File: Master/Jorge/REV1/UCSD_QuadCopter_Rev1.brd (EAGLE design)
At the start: 71.7 x 73.6 mm, 58 parts, among them J1 ISP, K1 653002114822, K2 653002114822, K3 653002114822, K4 653002114822, U1 ATMEGA128RFA1, U2 TPS73633-DBVT, U3 SI2302CDS-T1-E3, U4 LSM9DS0, U5 SI2302CDS-T1-E3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

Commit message: Uploading Finished QuadCopter PCB REV1
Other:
- board size 71.7 x 73.6 mm -> 99.8 x 99.9 mm
- board text added: "0.276 inch 7.0104 mm"
- board text added: "3.930 inch 99.822 mm"
- board text added: "3.934 inch 99.9236 mm"
- board text added: ">Info Board Name: UCSD QuadCopter Part Number: 0 Number of Layers: 2 Dimension X= 3.930 inch Dimension Y= 3.934 inch Board Material Type: FR-4 Solder Mask Color: Green Silkscreen Color: White Finish Plating: HASAL Revision Number: 1"
- board text removed: "0.238 inch 6.045 mm"
- board text removed: "2.83 inch 71.88 mm"
- board text removed: "2.90 inch 73.66 mm"
- board text removed: ">Info Board Name: UCSD QuadCopter Part Number: 0 Number of Layers: 2 Dimension X= 2.83 inch Dimension Y= 2.90 inch Board Material Type: FR-4 Solder Mask Color: Green Silkscreen Color: White Finish Plating: HASAL Revision Number: 1"

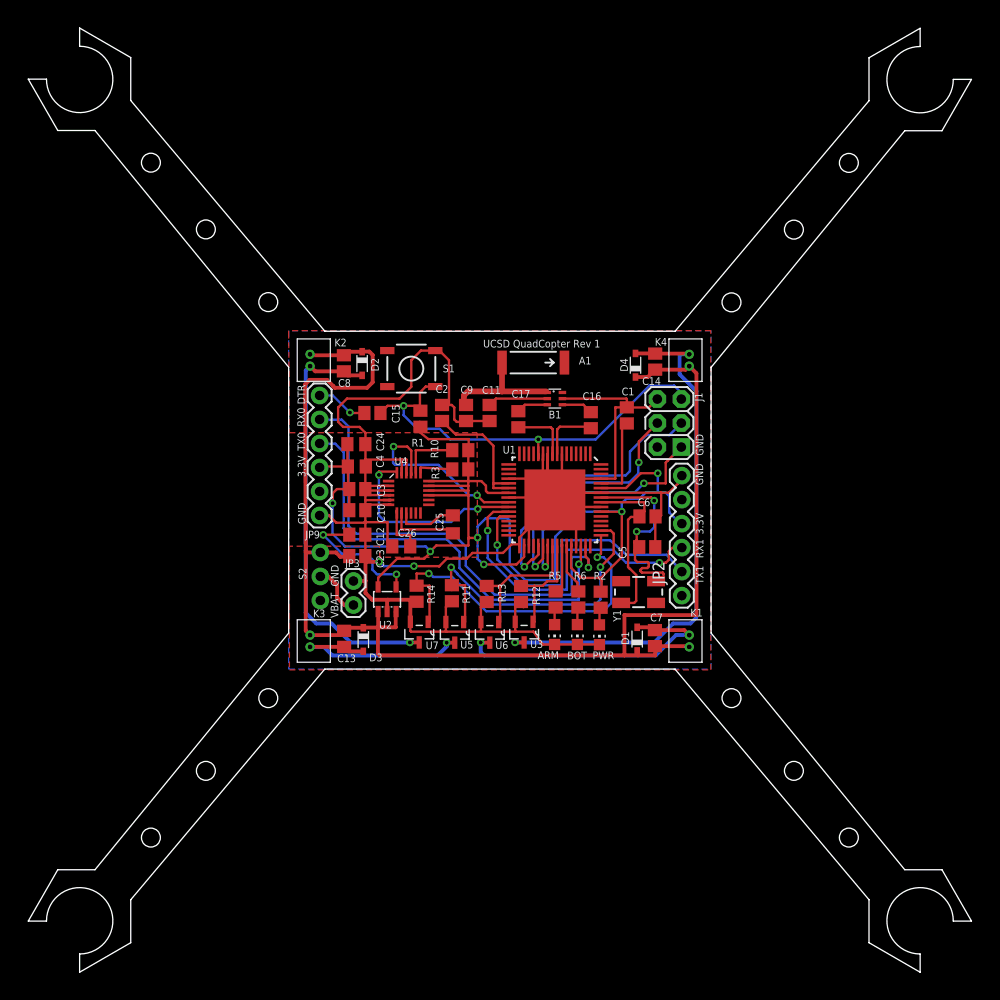
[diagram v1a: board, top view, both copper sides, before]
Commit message: Latest Multiwii Code & Schematic
Uploading latest code & Schematic (Jorge).
+ Correct IMU ACC & GYRO ORENTATIOn.
+ Adding some parameters to EEPROM by default..
+ Correct Motors Pin Output for (Rear_L, Rear_R, Front_L, Front_R)
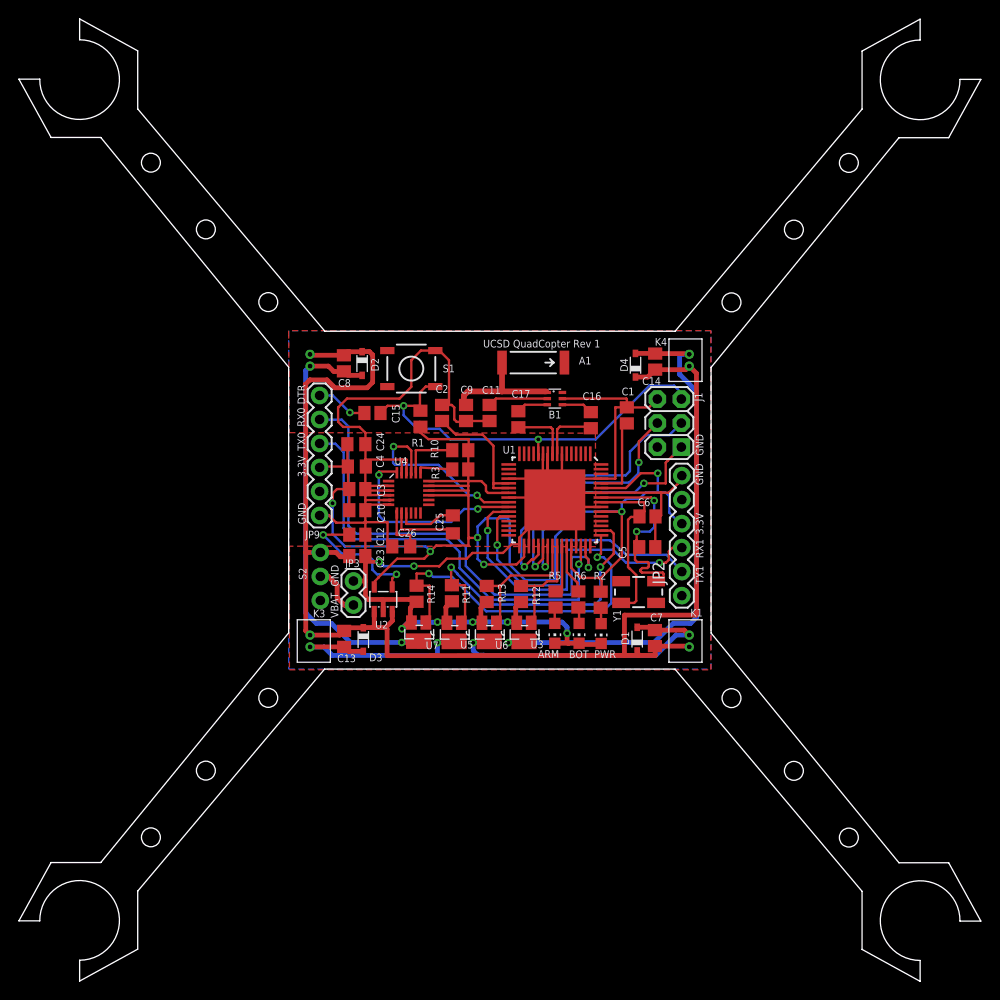
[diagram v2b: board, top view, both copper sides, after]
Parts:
- C10: value 1uF -> 200uF
- C23: value 1uF -> 100uF
- moved U2 0.41 mm to (10.0, 7.39)
- moved BOT 0.22 mm to (30.7, 3.78)
- moved PWR 0.22 mm to (33.1, 3.76)
- moved ARM 0.13 mm to (28.2, 3.78)
- moved U3 0.06 mm to (25.0, 3.89)
- flipped K2 to the bottom
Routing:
- net GND: track 246.1 -> 249.0 mm, vias 2 -> 7
- net N$32: track 56.6 -> 58.0 mm
- net VBAT: track 145.3 -> 143.9 mm
- net N$29: track 31.0 -> 32.4 mm
- net N$31: track 22.3 -> 22.9 mm
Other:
- board size 99.8 x 99.9 mm -> 101.8 x 101.9 mm
